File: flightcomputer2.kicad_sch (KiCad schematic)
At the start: 0 parts

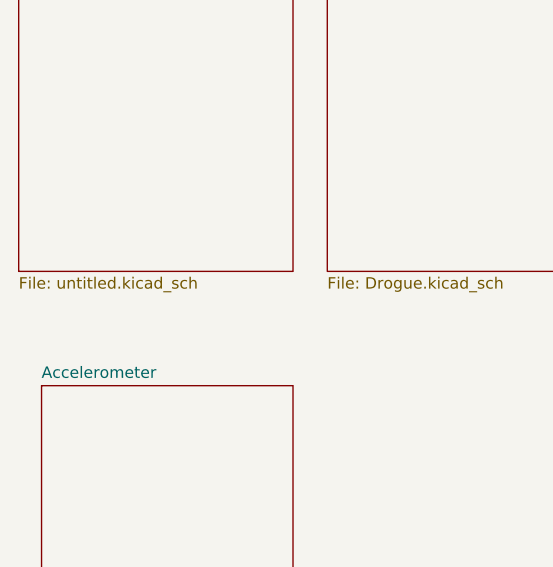
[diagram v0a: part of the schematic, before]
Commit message: began fixing schematic added barometer
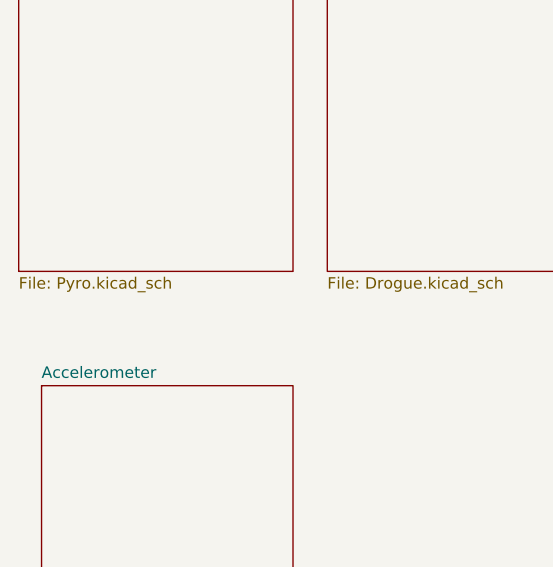
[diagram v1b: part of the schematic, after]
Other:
- sheet Pyro: file untitled.kicad_sch -> Pyro.kicad_sch
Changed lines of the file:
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@@
 			)
 		)
-		(property "Sheetfile" "untitled.kicad_sch"
+		(property "Sheetfile" "Pyro.kicad_sch"
 			(at 24.13 130.1246 0)
 			(effects
